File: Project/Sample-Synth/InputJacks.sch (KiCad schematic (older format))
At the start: 6 parts

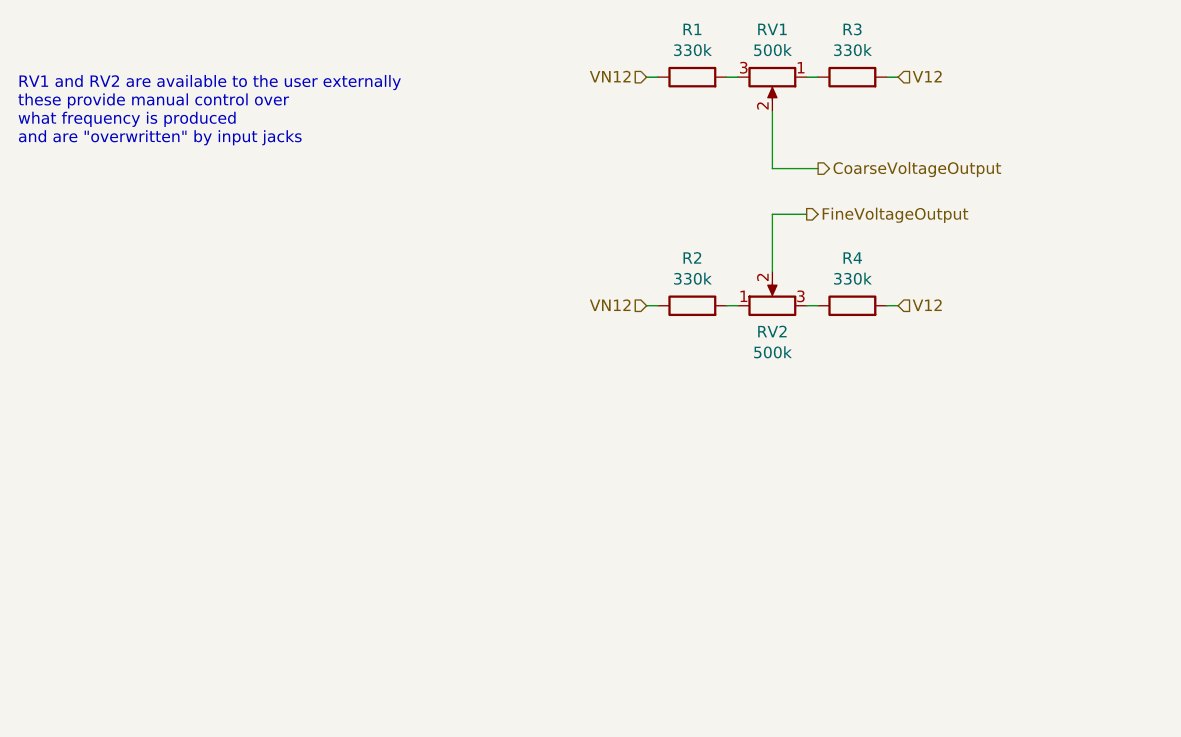
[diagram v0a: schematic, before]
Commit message: Updates and Datasheets
Included datasheets for parts chosen (so far!). Updated main schematic, separated input jacks to separate page.
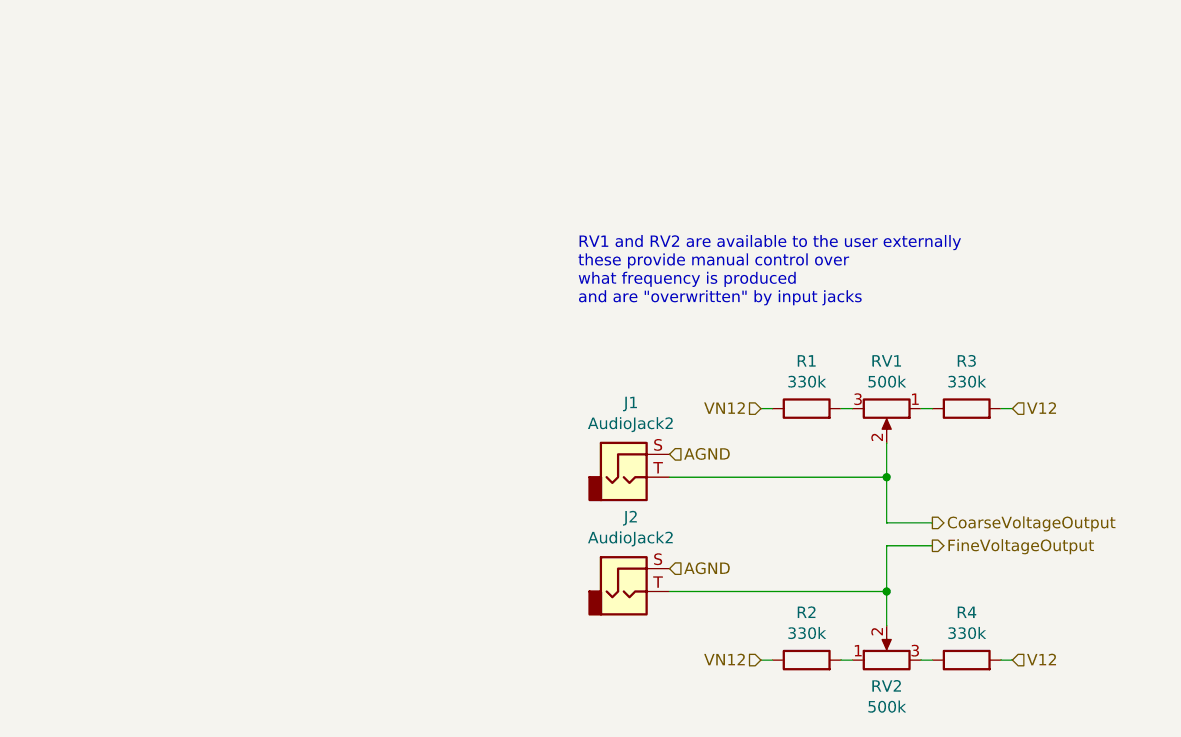
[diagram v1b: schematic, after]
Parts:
- added J1, J2: AudioJack2, symbol Connector:AudioJack2
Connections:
- net CoarseVoltageOutput: now also J1.T
- net FineVoltageOutput: now also J2.T
- new net AGND: J1.S, J2.S
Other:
- moved on the sheet: R1, R2, R3, R4, RV1, RV2
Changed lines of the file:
@@
 Comment4 ""
 $EndDescr
-Text HLabel 5800 2700 2    50   Output ~ 0
+Text HLabel 6300 4250 2    50   Output ~ 0
 CoarseVoltageOutput
 $Comp
 L Device:R R?
 U 1 1 60CCA604
-P 5250 2300
+P 5750 3750
 AR Path="/60A84A0D/60CCA604" Ref="R?"  Part="1"
 AR Path="/60AC03A1/60CCA604" Ref="R1"  Part="1"
-F 0 "R1" V 5457 2300 50  0000 C CNN
-F 1 "330k" V 5366 2300 50  0000 C CNN
-F 2 "" V 5180 2300 50  0001 C CNN
-F 3 "~" H 5250 2300 50  0001 C CNN
-	1    5250 2300
+F 0 "R1" V 5957 3750 50  0000 C CNN
+F 1 "330k" V 5866 3750 50  0000 C CNN
+F 2 "" V 5680 3750 50  0001 C CNN
+F 3 "~" H 5750 3750 50  0001 C CNN
+	1    5750 3750
 	0    -1   -1   0
 $EndComp
@@
 L Device:R R?
 U 1 1 60CCA60A
-P 5950 2300
+P 6450 3750
 AR Path="/60A84A0D/60CCA60A" Ref="R?"  Part="1"
 AR Path="/60AC03A1/60CCA60A" Ref="R3"  Part="1"
-F 0 "R3" V 6157 2300 50  0000 C CNN
-F 1 "330k" V 6066 2300 50  0000 C CNN
-F 2 "" V 5880 2300 50  0001 C CNN
-F 3 "~" H 5950 2300 50  0001 C CNN
-	1    5950 2300
+F 0 "R3" V 6657 3750 50  0000 C CNN
+F 1 "330k" V 6566 3750 50  0000 C CNN
+F 2 "" V 6380 3750 50  0001 C CNN
+F 3 "~" H 6450 3750 50  0001 C CNN
+	1    6450 3750
 	0    -1   -1   0
 $EndComp
@@
 L Device:R_POT RV?
 U 1 1 60CCA610
-P 5600 2300
+P 6100 3750
 AR Path="/60A84A0D/60CCA610" Ref="RV?"  Part="1"
 AR Path="/60AC03A1/60CCA610" Ref="RV1"  Part="1"
-F 0 "RV1" V 5393 2300 50  0000 C CNN
-F 1 "500k" V 5484 2300 50  0000 C CNN
-F 2 "" H 5600 2300 50  0001 C CNN
-F 3 "~" H 5600 2300 50  0001 C CNN
-	1    5600 2300
+F 0 "RV1" V 5893 3750 50  0000 C CNN
+F 1 "500k" V 5984 3750 50  0000 C CNN
+F 2 "" H 6100 3750 50  0001 C CNN
+F 3 "~" H 6100 3750 50  0001 C CNN
+	1    6100 3750
 	0    1    1    0
 $EndComp
 Wire Wire Line
-	6150 2300 6100 2300
+	6650 3750 6600 3750
 Wire Wire Line
-	5100 2300 5050 2300
+	5600 3750 5550 3750
 Wire Wire Line
-	5800 2300 5750 2300
+	6300 3750 6250 3750
 Wire Wire Line
-	5400 2300 5450 2300
+	5900 3750 5950 3750
 Wire Wire Line
-	5600 2450 5600 2700
-Text HLabel 6150 2300 2    50   Input ~ 0
+	6100 3900 6100 4050
+Text HLabel 6650 3750 2    50   Input ~ 0
 V12
-Text HLabel 5050 2300 0    50   Input ~ 0
+Text HLabel 5550 3750 0    50   Input ~ 0
 VN12
 $Comp
 L Device:R R?
 U 1 1 60CCF288
-P 5250 3300
+P 5750 4850
 AR Path="/60A84A0D/60CCF288" Ref="R?"  Part="1"
 AR Path="/60AC03A1/60CCF288" Ref="R2"  Part="1"
-F 0 "R2" V 5457 3300 50  0000 C CNN
-F 1 "330k" V 5366 3300 50  0000 C CNN
-F 2 "" V 5180 3300 50  0001 C CNN
-F 3 "~" H 5250 3300 50  0001 C CNN
-	1    5250 3300
+F 0 "R2" V 5957 4850 50  0000 C CNN
+F 1 "330k" V 5866 4850 50  0000 C CNN
+F 2 "" V 5680 4850 50  0001 C CNN
+F 3 "~" H 5750 4850 50  0001 C CNN
+	1    5750 4850
 	0    -1   -1   0
 $EndComp
@@
 L Device:R R?
 U 1 1 60CCF28E
-P 5950 3300
+P 6450 4850
 AR Path="/60A84A0D/60CCF28E" Ref="R?"  Part="1"
 AR Path="/60AC03A1/60CCF28E" Ref="R4"  Part="1"
-F 0 "R4" V 6157 3300 50  0000 C CNN
-F 1 "330k" V 6066 3300 50  0000 C CNN
-F 2 "" V 5880 3300 50  0001 C CNN
-F 3 "~" H 5950 3300 50  0001 C CNN
-	1    5950 3300
+F 0 "R4" V 6657 4850 50  0000 C CNN
+F 1 "330k" V 6566 4850 50  0000 C CNN
+F 2 "" V 6380 4850 50  0001 C CNN
+F 3 "~" H 6450 4850 50  0001 C CNN
+	1    6450 4850
 	0    -1   -1   0
 $EndComp
@@
 L Device:R_POT RV?
 U 1 1 60CCF294
-P 5600 3300
+P 6100 4850
 AR Path="/60A84A0D/60CCF294" Ref="RV?"  Part="1"
 AR Path="/60AC03A1/60CCF294" Ref="RV2"  Part="1"
-F 0 "RV2" V 5485 3300 50  0000 C CNN
-F 1 "500k" V 5394 3300 50  0000 C CNN
-F 2 "" H 5600 3300 50  0001 C CNN
-F 3 "~" H 5600 3300 50  0001 C CNN
-	1    5600 3300
+F 0 "RV2" V 5985 4850 50  0000 C CNN
+F 1 "500k" V 5894 4850 50  0000 C CNN
+F 2 "" H 6100 4850 50  0001 C CNN
+F 3 "~" H 6100 4850 50  0001 C CNN
+	1    6100 4850
 	0    -1   -1   0
 $EndComp
 Wire Wire Line
-	5100 3300 5050 3300
+	5600 4850 5550 4850
 Wire Wire Line
-	6100 3300 6150 3300
+	6600 4850 6650 4850
 Wire Wire Line
-	5750 3300 5800 3300
+	6250 4850 6300 4850
 Wire Wire Line
-	5450 3300 5400 3300
-Text HLabel 5050 3300 0    50   Input ~ 0
+	5950 4850 5900 4850
+Text HLabel 5550 4850 0    50   Input ~ 0
 VN12
-Text HLabel 6150 3300 2    50   Input ~ 0
+Text HLabel 6650 4850 2    50   Input ~ 0
 V12
-Text Notes 2300 2600 0    50   ~ 0
+Text Notes 4750 3300 0    50   ~ 0
 RV1 and RV2 are available to the user externally\nthese provide manual control over\nwhat frequency is produced\nand are "overwritten" by input jacks
-Text HLabel 5750 2900 2    50   Output ~ 0
+Text HLabel 6300 4350 2    50   Output ~ 0
 FineVoltageOutput
 Wire Wire Line
-	5800 2700 5600 2700
+	6300 4250 6100 4250
 Wire Wire Line
-	5750 2900 5600 2900
+	6100 4350 6100 4550
+$Comp
+L Connector:AudioJack2 J1
+U 1 1 60ADB241
+P 4950 4050
+F 0 "J1" H 4982 4375 50  0000 C CNN
+F 1 "AudioJack2" H 4982 4284 50  0000 C CNN
+F 2 "" H 4950 4050 50  0001 C CNN
+F 3 "~" H 4950 4050 50  0001 C CNN
+	1    4950 4050
+	1    0    0    -1
+$EndComp
+$Comp
+L Connector:AudioJack2 J2
+U 1 1 60ADE2D3
+P 4950 4550
+F 0 "J2" H 4982 4875 50  0000 C CNN
+F 1 "AudioJack2" H 4982 4784 50  0000 C CNN
+F 2 "" H 4950 4550 50  0001 C CNN
+F 3 "~" H 4950 4550 50  0001 C CNN
+	1    4950 4550
+	1    0    0    -1
+$EndComp
+Text HLabel 5150 4450 2    50   Input ~ 0
+AGND
+Text HLabel 5150 3950 2    50   Input ~ 0
+AGND
 Wire Wire Line
-	5600 2900 5600 3150
+	5150 4050 6100 4050
+Connection ~ 6100 4050
+Wire Wire Line
+	5150 4550 6100 4550
+Wire Wire Line
+	6100 4350 6300 4350
+Wire Wire Line
+	6100 4550 6100 4700
+Connection ~ 6100 4550
+Wire Wire Line
+	6100 4050 6100 4250
 $EndSCHEMATC
